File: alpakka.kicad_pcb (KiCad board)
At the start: 2 copper layers, 130 x 51 mm, 126 parts, among them J3 Debug, J4 USB_C_Receptacle_USB2.0, P1 Debug, P2 Endpoint, P3 Conn_01x02, Q1 Q_PMOS_DGS, SW1 SW_MEC_5G, U1 Raspberry_Pico, U10 ST_LSM6, U11 LP2985-3.3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

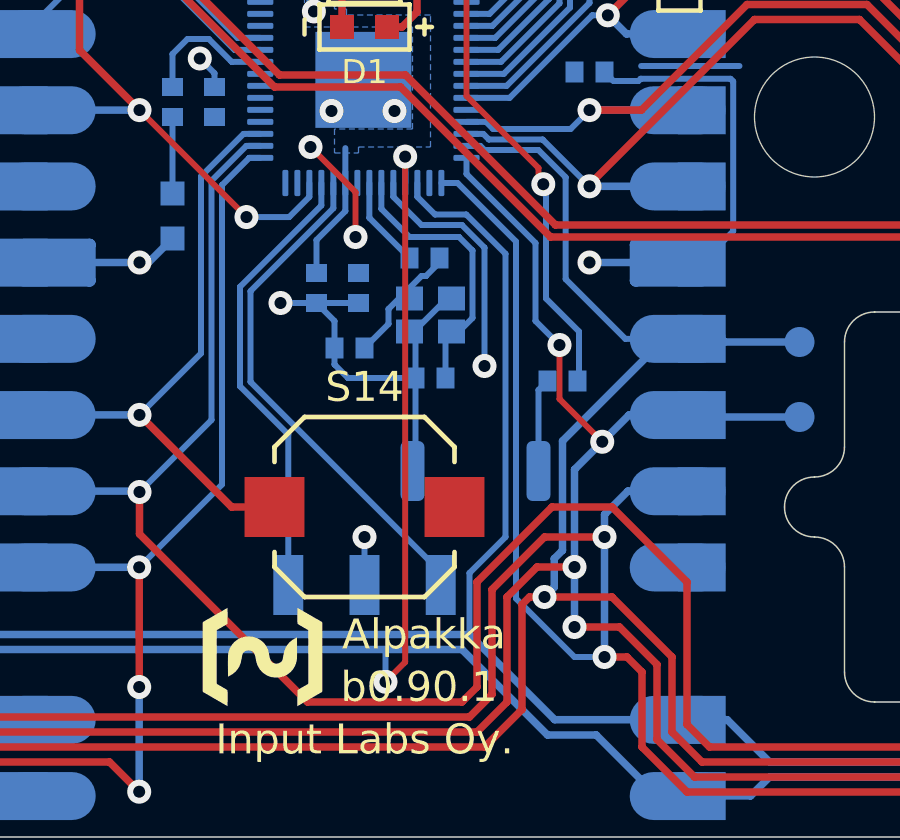
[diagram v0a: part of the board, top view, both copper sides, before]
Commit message: changed crystal to a more common size
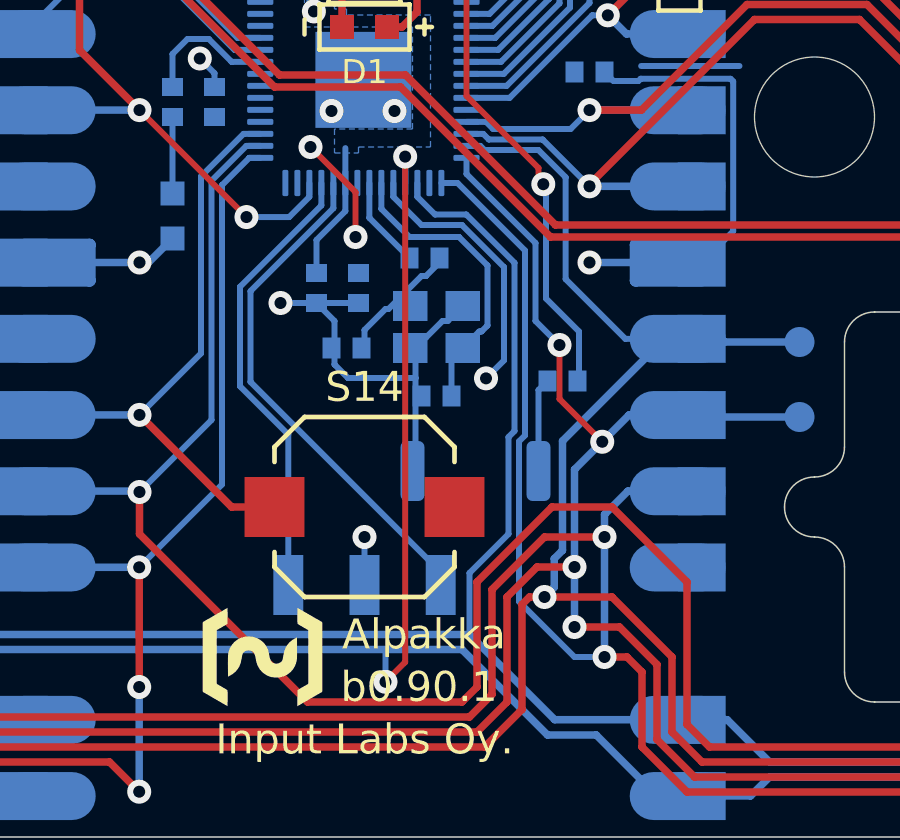
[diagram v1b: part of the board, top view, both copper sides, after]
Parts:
- Y1: footprint Crystal:Crystal_SMD_2016-4Pin_2.0x1.6mm -> Crystal:Crystal_SMD_2520-4Pin_2.5x2.0mm
- moved C8 0.63 mm to (102.4, 71.3)
- moved Y1 0.45 mm to (102.4, 69.0)
- moved C9 0.10 mm to (99.4, 69.7)
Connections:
- SW1 pad 2: (no net) -> GND
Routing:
- net Net-(U5-XIN): track 9.24 -> 10.1 mm
- net GND: track 301.0 -> 301.8 mm
